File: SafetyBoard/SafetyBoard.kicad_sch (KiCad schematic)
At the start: 0 parts

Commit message: Changed a buncha stuff on other ppl's board. established new branch
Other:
- added sheet BSPD (../BSPD/BSPD/BSPD.kicad_sch)
- added sheet LATCH (../LATCH/LATCH/LATCH.kicad_sch)
- added sheet TSSI (../TSSI/TSSI/TSSI.kicad_sch)
- added sheet Untitled Sheet (../PDB/v2026.1/Kicad/PowerDistributionBoard.kicad_sch)

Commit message: day 2 grind
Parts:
- added F1, F2, F3, F4, F5, F6: ~, 0footprints:FUSE_3522-2, symbol Device:Fuse
- added J1: ESTOP/SDC switch, 0footprints:Molex_Mini-Fit_Jr_5566-02A_2x01_P4.20mm_Vertical, symbol Connector_Generic:Conn_02x01
- added J2, J3: SDC OUT, 0footprints:Molex_Mini-Fit_Jr_5566-02A_2x01_P4.20mm_Vertical, symbol Connector_Generic:Conn_02x01
- added J4, J7: ACCU, 0footprints:Molex_Mini-Fit_Jr_5566-04A_2x02_P4.20mm_Vertical, symbol Connector_Generic:Conn_02x02_Top_Bottom
- added J5: BSPD, 0footprints:Molex_Mini-Fit_Jr_5566-06A_2x03_P4.20mm_Vertical, symbol Connector_Generic:Conn_02x03_Top_Bottom
- added J6: LATCH, 0footprints:Molex_Mini-Fit_Jr_5566-08A_2x04_P4.20mm_Vertical, symbol Connector_Generic:Conn_02x04_Top_Bottom
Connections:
- net BSPD/12V: now also F1.1
- net LATCH/GVLM_OUTPUT: now also J1.1 (Pin_1)
- net TSSI/GLV: now also F5.1
- new net: F6.1, J4.1 (Pin_1)
- new net: J1.2 (Pin_2), J2.1 (Pin_1), J2.2 (Pin_2)
- new net 12V: F1.2, F2.2, F3.2, F5.2, F6.2
- new net 24V: F4.2, J3.1 (Pin_1)
- new net BMS FAULT: J4.4 (Pin_4)
- new net CCM Helper/12V: F3.1
- new net CCM Helper/24V: F4.1
- new net GND: J3.2 (Pin_2), J4.2 (Pin_2)
- new net IMD Fault: J4.3 (Pin_3)
- new net LATCH/12V: F2.1
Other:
- removed sheet Untitled Sheet
- added sheet CCM Helper (CCMIO.kicad_sch)
- added sheet DCDC CONVERTERS (./24V DC-DC Converter 2/24V DC-DC Converter.kicad_sch)
- sheet BSPD ports: added none; removed Current Sensor
- sheet LATCH ports: added 12V, IMD_FAULT; removed none
- sheet TSSI ports: added none; removed GREEN_LED, RED_LED

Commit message: hopefully this lets avadi pull
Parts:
- removed J5: BSPD, 0footprints:Molex_Mini-Fit_Jr_5566-06A_2x03_P4.20mm_Vertical, symbol Connector_Generic:Conn_02x03_Top_Bottom
- removed J6: LATCH, 0footprints:Molex_Mini-Fit_Jr_5566-08A_2x04_P4.20mm_Vertical, symbol Connector_Generic:Conn_02x04_Top_Bottom
- removed J7: ACCU, 0footprints:Molex_Mini-Fit_Jr_5566-04A_2x02_P4.20mm_Vertical, symbol Connector_Generic:Conn_02x02_Top_Bottom
- added F10, F7, F8, F9: ~, 0footprints:FUSE_3522-2, symbol Device:Fuse
- added J4, J7: 12v EXP, 0footprints:Molex_Mini-Fit_Jr_5566-02A_2x01_P4.20mm_Vertical, symbol Connector_Generic:Conn_02x01
- added J6: 24v EXP, 0footprints:Molex_Mini-Fit_Jr_5566-02A_2x01_P4.20mm_Vertical, symbol Connector_Generic:Conn_02x01
- J5: renamed from J3; value SDC OUT -> PWR IN
- renumbered J4 to J3
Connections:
- net 12V: now also F7.1
- net 24V: now also F8.1, F9.1; no longer J5.1 (Pin_1)
- net GND: now also J4.2 (Pin_2), J6.2 (Pin_2), J7.2 (Pin_2)
- new net: F7.2, J4.1 (Pin_1)
- new net: F9.2, J6.1 (Pin_1)
- new net: F8.2, J5.1 (Pin_1)
- new net: F10.2, J7.1 (Pin_1)
- new net 5V: F10.1
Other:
- sheet DCDC CONVERTERS ports: added 12V_OUT, 24V_IN, 5V; removed none
- moved on the sheet: J5

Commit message: rough layout done
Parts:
- J7: value 12v EXP -> 5v EXP
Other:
- sheet CCM Helper ports: added BPS1 OUT; removed BPS1_OUT
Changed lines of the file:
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@@
+	(wire
+		(pts
+			(xy 72.898 177.8) (xy 75.184 177.8)
+		)
+		(stroke
+			(width 0)
+			(type default)
+		)
+	)
 	(wire
 		(pts
@@
 		(pts
 			(xy 93.98 49.276) (xy 85.852 49.276)
-		)
-		(stroke
-			(width 0)
-			(type default)
-		)
-	)
-	(wire
-		(pts
-			(xy 74.93 177.8) (xy 72.898 177.8)
 		)
 		(stroke
@@
 	)
 	(label "24V"
+		(at 74.676 184.912 0)
+		(effects
+			(font
+				(size 1.27 1.27)
+			)
+			(justify left bottom)
+		)
+	)
+	(label "24V"
 		(at 228.854 33.02 180)
 		(effects
@@
 	)
 	(label "12V"
+		(at 75.184 177.8 0)
+		(effects
+			(font
+				(size 1.27 1.27)
+			)
+			(justify left bottom)
+		)
+	)
+	(label "12V"
 		(at 227.584 49.784 180)
 		(effects
@@
 		)
 	)
-	(label "24V"
-		(at 74.93 177.8 0)
-		(effects
-			(font
-				(size 1.27 1.27)
-			)
-			(justify left bottom)
-		)
-	)
 	(label "5V"
 		(at 72.898 180.848 0)
@@
 	)
 	(label "12V"
-		(at 74.676 184.912 0)
-		(effects
-			(font
-				(size 1.27 1.27)
-			)
-			(justify left bottom)
-		)
-	)
-	(label "12V"
 		(at 67.056 137.414 180)
 		(effects
@@
 			)
 		)
-		(property "Value" "12v EXP"
+		(property "Value" "5v EXP"
 			(at 243.078 59.182 0)
 			(effects
@@
 			)
 		)
-		(pin "BPS1_OUT" input
-			(at 93.98 49.276 180)
-			(effects
-				(font
-					(size 1.27 1.27)
-				)
-				(justify left)
-			)
-		)
 		(pin "CCM fdbk" input
 			(at 128.016 49.53 0)
@@
 			)
 		)
+		(pin "BPS1 OUT" input
+			(at 93.98 49.276 180)
+			(effects
+				(font
+					(size 1.27 1.27)
+				)
+				(justify left)
+			)
+		)

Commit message: silkscreen and some fuses or something
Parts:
- removed F1, F5: ~, 0footprints:FUSE_3522-2, symbol Device:Fuse
- added F1, F5: 2A, Fuse:Fuse_2920_7451Metric_Pad2.10x5.45mm_HandSolder, symbol Device:Polyfuse
- F3: value ~ -> 5A MAX
- F4, F8, F9: value ~ -> 10A MAX
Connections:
- net 12V: now also F1.1, F5.1
- net BSPD/12V: now also F1.2
- net TSSI/GLV: now also F5.2
- net at J1.2 (Pin_2), J2.2 (Pin_2): no longer J2.1 (Pin_1)
- no-connect marks 0 -> 1
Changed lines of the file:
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@@
 	(generator_version "9.0")
 	(paper "A4")
-	(junction
-		(at 152.908 140.208)
-		(diameter 0)
-		(color 0 0 0 0)
+	(no_connect
+		(at 154.432 140.208)
 	)
 	(wire
@@
 	(wire
 		(pts
-			(xy 154.432 140.208) (xy 152.908 140.208)
-		)
-		(stroke
-			(width 0)
-			(type default)
-		)
-	)
-	(wire
-		(pts
 			(xy 139.7 46.99) (xy 139.7 55.88)
 		)
@@
 		(pts
 			(xy 129.032 99.06) (xy 129.032 105.41)
+		)
+		(stroke
+			(width 0)
+			(type default)
+		)
+	)
+	(wire
+		(pts
+			(xy 46.99 71.374) (xy 47.244 71.374)
 		)
 		(stroke
@@
 	)
 	(label "12V"
-		(at 46.99 71.374 180)
+		(at 47.244 71.374 180)
 		(effects
 			(font
@@
 	(symbol
 		(lib_id "Device:Fuse")
-		(at 50.8 71.374 270)
-		(unit 1)
-		(exclude_from_sim no)
-		(in_bom yes)
-		(on_board yes)
-		(dnp no)
-		(property "Reference" "F1"
-			(at 50.8 73.66 90)
-			(effects
-				(font
-					(size 1.27 1.27)
-				)
-			)
-		)
-		(property "Value" "~"
-			(at 50.8 69.596 90)
-			(effects
-				(font
-					(size 1.27 1.27)
-				)
-			)
-		)
-		(property "Footprint" "0footprints:FUSE_3522-2"
-			(at 50.8 69.596 90)
-			(effects
-				(font
-					(size 1.27 1.27)
-				)
-				(hide yes)
-			)
-		)
-		(property "Datasheet" "https://www.keyelco.com/userAssets/file/M65p41.pdf"
-			(at 50.8 71.374 0)
-			(effects
-				(font
-					(size 1.27 1.27)
-				)
-				(hide yes)
-			)
-		)
-		(property "Description" "Fuse"
-			(at 50.8 71.374 0)
-			(effects
-				(font
-					(size 1.27 1.27)
-				)
-				(hide yes)
-			)
-		)
-		(pin "1"
-		)
-		(pin "2"
-		)
-		(instances
-			(project "SafetyBoard"
-				(path "/30d029c6-868b-41ac-953d-167a7d76c1a3"
-					(reference "F1")
-					(unit 1)
-				)
-			)
-		)
-	)
-	(symbol
-		(lib_id "Device:Fuse")
 		(at 210.566 125.73 270)
 		(unit 1)
@@
 			)
 		)
-		(property "Value" "~"
+		(property "Value" "10A MAX"
 			(at 131.826 37.846 90)
 			(effects
@@
 	)
 	(symbol
+		(lib_id "Device:Polyfuse")
+		(at 180.086 67.056 270)
+		(unit 1)
+		(exclude_from_sim no)
+		(in_bom yes)
+		(on_board yes)
+		(dnp no)
+		(fields_autoplaced yes)
+		(property "Reference" "F5"
+			(at 180.086 61.214 90)
+			(effects
+				(font
+					(size 1.27 1.27)
+				)
+			)
+		)
+		(property "Value" "2A"
+			(at 180.086 63.754 90)
+			(effects
+				(font
+					(size 1.27 1.27)
+				)
+			)
+		)
+		(property "Footprint" "Fuse:Fuse_2920_7451Metric_Pad2.10x5.45mm_HandSolder"
+			(at 175.006 68.326 0)
+			(effects
+				(font
+					(size 1.27 1.27)
+				)
+				(justify left)
+				(hide yes)
+			)
+		)
+		(property "Datasheet" "~"
+			(at 180.086 67.056 0)
+			(effects
+				(font
+					(size 1.27 1.27)
+				)
+				(hide yes)
+			)
+		)
+		(property "Description" "Resettable fuse, polymeric positive temperature coefficient"
+			(at 180.086 67.056 0)
+			(effects
+				(font
+					(size 1.27 1.27)
+				)
+				(hide yes)
+			)
+		)
+		(property "MPN" "SMD2920B200TF/24 "
+			(at 180.086 67.056 0)
+			(effects
+				(font
+					(size 1.27 1.27)
+				)
+				(hide yes)
+			)
+		)
+		(property "MFG" "YAGEO"
+			(at 180.086 67.056 0)
+			(effects
+				(font
+					(size 1.27 1.27)
+				)
+				(hide yes)
+			)
+		)
+		(pin "2"
+		)
+		(pin "1"
+		)
+		(instances
+			(project "SafetyBoard"
+				(path "/30d029c6-868b-41ac-953d-167a7d76c1a3"
+					(reference "F5")
+					(unit 1)
+				)
+			)
+		)
+	)
+	(symbol
 		(lib_id "power:GND")
 		(at 248.412 17.272 0)
@@
 			)
 		)
-		(property "Value" "~"
+		(property "Value" "5A MAX"
 			(at 131.826 33.274 90)
 			(effects
@@
 			)
 		)
-		(property "Value" "~"
+		(property "Value" "10A MAX"
 			(at 231.902 19.05 90)
 			(effects
@@
 	)
 	(symbol
-		(lib_id "Device:Fuse")
-		(at 180.086 67.056 90)
-		(unit 1)
-		(exclude_from_sim no)
-		(in_bom yes)
-		(on_board yes)
-		(dnp no)
-		(property "Reference" "F5"
-			(at 180.086 64.77 90)
-			(effects
-				(font
-					(size 1.27 1.27)
-				)
-			)
-		)
-		(property "Value" "~"
-			(at 180.086 68.834 90)
-			(effects
-				(font
-					(size 1.27 1.27)
-				)
-			)
-		)
-		(property "Footprint" "0footprints:FUSE_3522-2"
-			(at 180.086 68.834 90)
-			(effects
-				(font
-					(size 1.27 1.27)
-				)
-				(hide yes)
-			)
-		)
-		(property "Datasheet" "https://www.keyelco.com/userAssets/file/M65p41.pdf"
-			(at 180.086 67.056 0)
-			(effects
-				(font
-					(size 1.27 1.27)
-				)
-				(hide yes)
-			)
-		)
-		(property "Description" "Fuse"
-			(at 180.086 67.056 0)
-			(effects
-				(font
-					(size 1.27 1.27)
-				)
-				(hide yes)
-			)
-		)
-		(pin "1"
-		)
-		(pin "2"
-		)
-		(instances
-			(project "SafetyBoard"
-				(path "/30d029c6-868b-41ac-953d-167a7d76c1a3"
-					(reference "F5")
-					(unit 1)
-				)
-			)
-		)
-	)
-	(symbol
 		(lib_id "Connector_Generic:Conn_02x01")
 		(at 240.792 17.272 0)
@@
 			)
 		)
-		(property "Value" "~"
+		(property "Value" "10A MAX"
 			(at 232.664 34.798 90)
 			(effects
@@
 					(unit 1)
 				)
+			)
+		)
+	)
+	(symbol
+		(lib_id "Device:Polyfuse")
+		(at 50.8 71.374 90)
+		(unit 1)
+		(exclude_from_sim no)
+		(in_bom yes)
+		(on_board yes)
+		(dnp no)
+		(fields_autoplaced yes)
+		(property "Reference" "F1"
+			(at 50.8 64.77 90)
+			(effects
+				(font
+					(size 1.27 1.27)
+				)
+			)
+		)
+		(property "Value" "2A"
+			(at 50.8 67.31 90)
+			(effects
+				(font
+					(size 1.27 1.27)
+				)
+			)
+		)
+		(property "Footprint" "Fuse:Fuse_2920_7451Metric_Pad2.10x5.45mm_HandSolder"
+			(at 55.88 70.104 0)
+			(effects
+				(font
+					(size 1.27 1.27)
+				)
+				(justify left)
+				(hide yes)
+			)
+		)
+		(property "Datasheet" "~"
+			(at 50.8 71.374 0)
+			(effects
+				(font
+					(size 1.27 1.27)
+				)
+				(hide yes)
+			)
+		)
+		(property "Description" "Resettable fuse, polymeric positive temperature coefficient"
+			(at 50.8 71.374 0)
+			(effects
+				(font
+					(size 1.27 1.27)
+				)
+				(hide yes)
+			)
+		)
+		(property "MPN" "SMD2920B200TF/24 "
+			(at 50.8 71.374 0)
+			(effects
+				(font
+					(size 1.27 1.27)
+				)
+				(hide yes)
+			)
+		)
+		(property "MFG" "YAGEO"
+			(at 50.8 71.374 0)
+			(effects
+				(font
+					(size 1.27 1.27)
+				)
+				(hide yes)
+			)
+		)
+		(pin "2"
+		)
+		(pin "1"
+		)
+		(instances
+			(project "SafetyBoard"
+				(path "/30d029c6-868b-41ac-953d-167a7d76c1a3"
+					(reference "F1")
+					(unit 1)
+				)

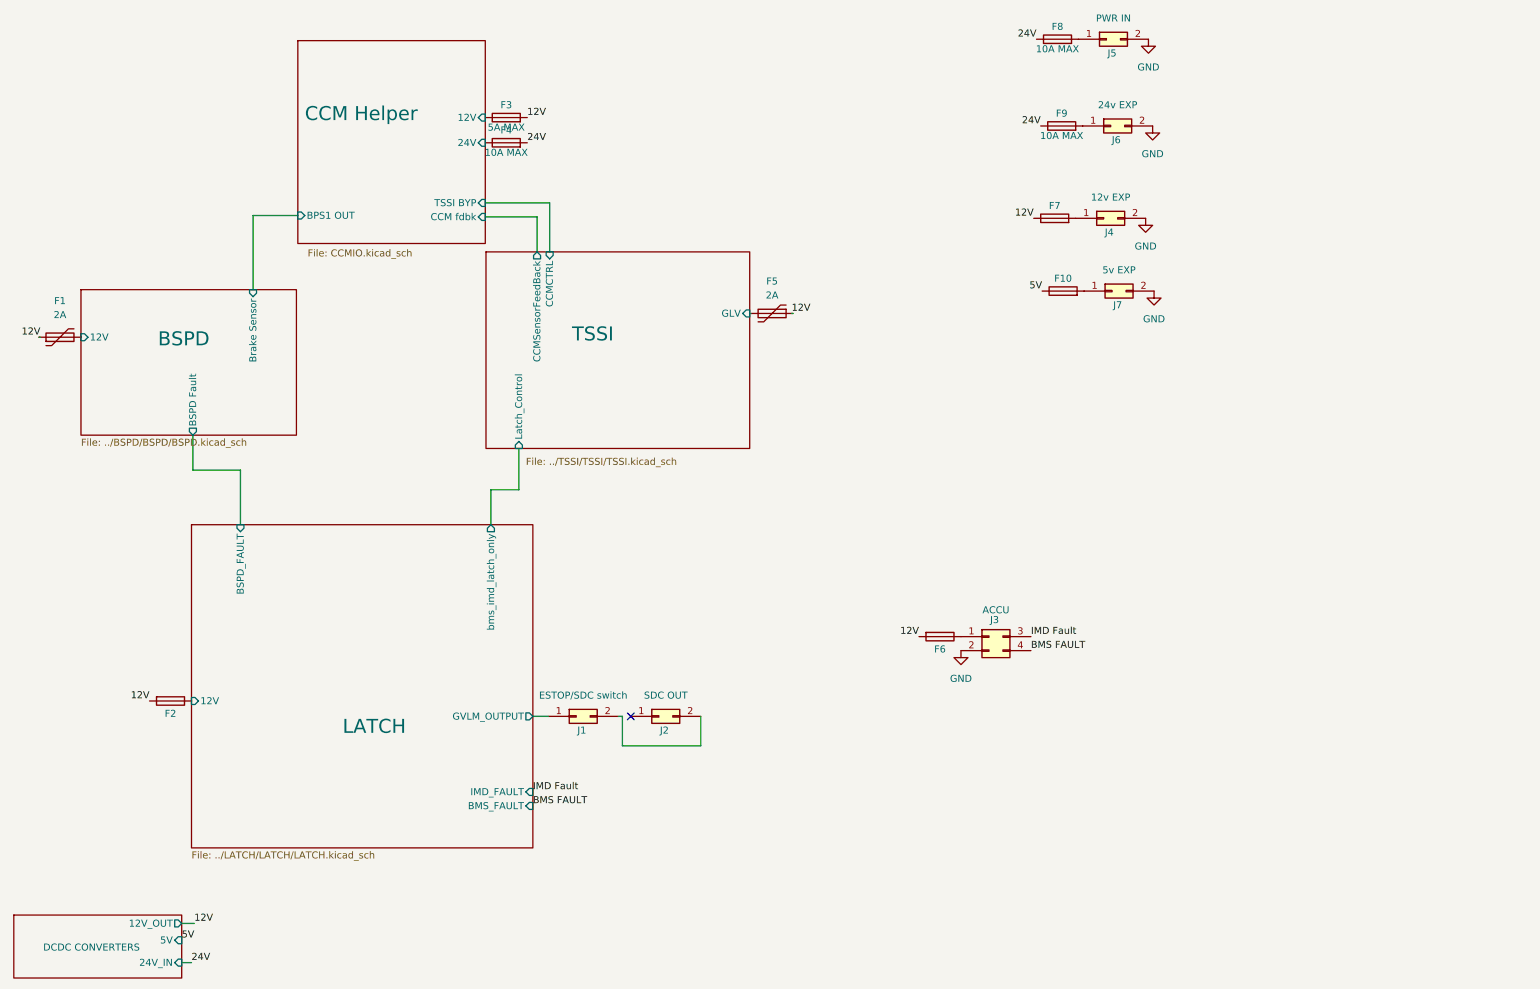
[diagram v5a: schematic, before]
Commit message: I think think this is final but need to defuck the BOM
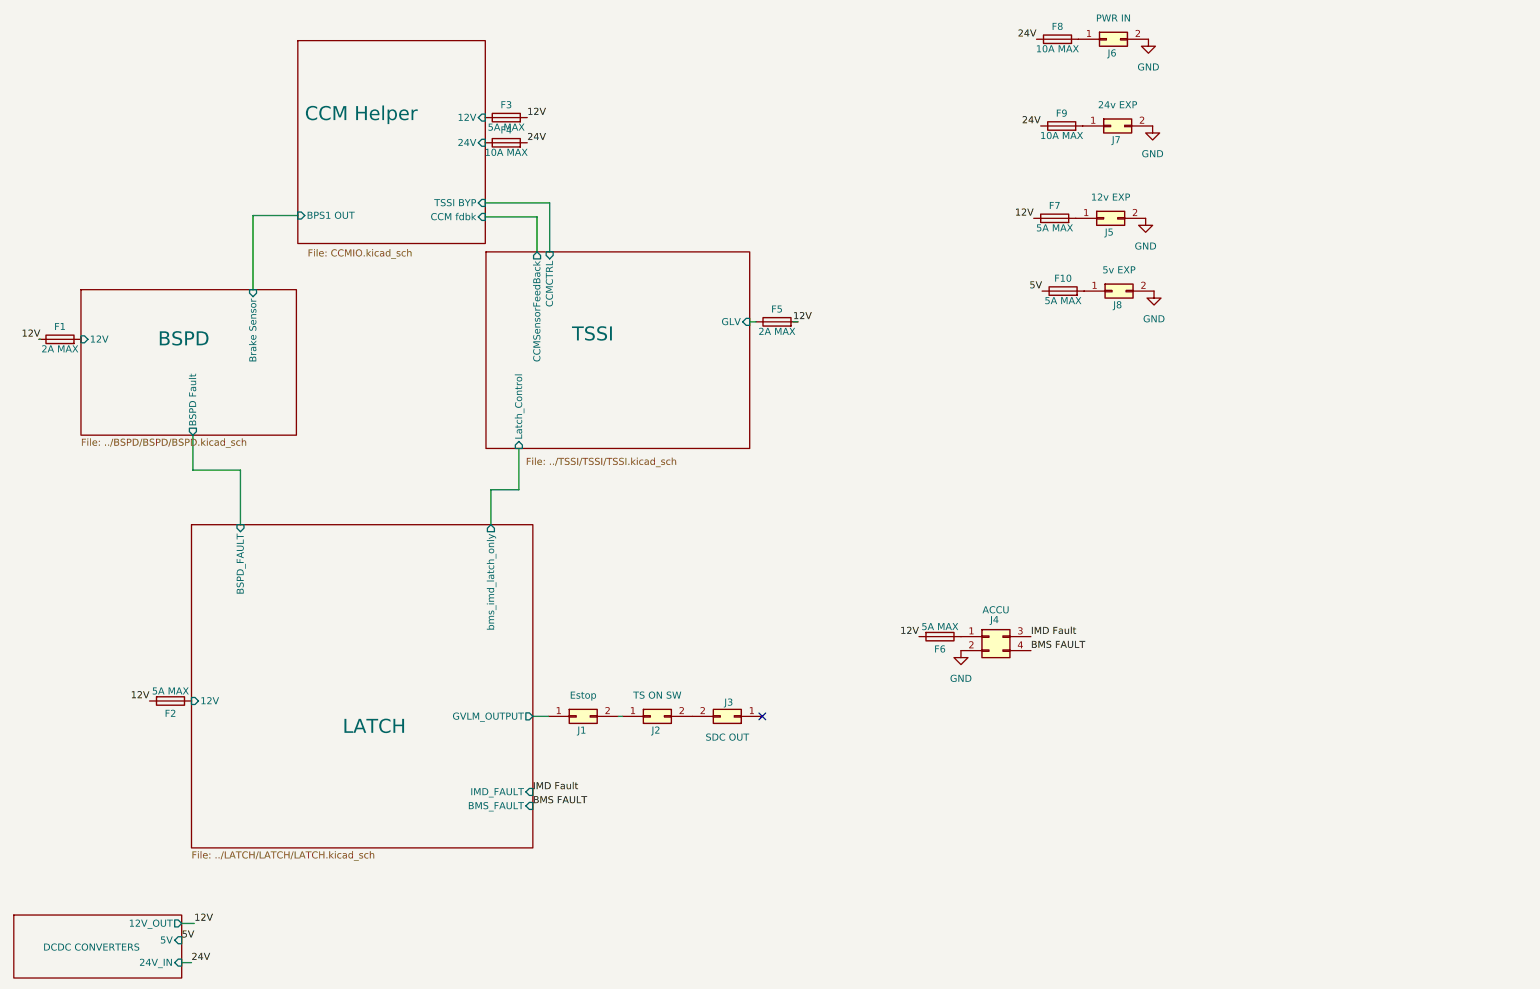
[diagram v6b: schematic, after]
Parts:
- removed F1, F5: 2A, Fuse:Fuse_2920_7451Metric_Pad2.10x5.45mm_HandSolder, symbol Device:Polyfuse
- added F1, F5: 2A MAX, 0footprints:FUSE_3522-2, symbol Device:Fuse
- added J2: TS ON SW, 0footprints:Molex_Mini-Fit_Jr_5566-02A_2x01_P4.20mm_Vertical, symbol Connector_Generic:Conn_02x01
- F10, F2, F6, F7: value ~ -> 5A MAX
- J1: value ESTOP/SDC switch -> Estop
- renumbered J2 to J3, J3 to J4, J4 to J5, J5 to J6, J6 to J7, J7 to J8
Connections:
- net 12V: now also F1.1, F5.2
- net BSPD/12V: now also F1.2
- net TSSI/GLV: now also F5.1
- net at J1.2 (Pin_2): now also J2.1 (Pin_1); no longer J3.2 (Pin_2)
- new net: J2.2 (Pin_2), J3.2 (Pin_2)
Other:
- moved on the sheet: J3

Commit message: Safety Board: added BOM and updated schematics
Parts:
- F1, F10, F2, F3, F4, F5, F6, F7, F8, F9: MFG (none) -> Littelfuse; MPN (none) -> 01530007Z
- J1, J2, J3, J5, J6, J7, J8: MFG (none) -> Molex; MPN (none) -> 0039310028
- J4: MFG (none) -> Molex; MPN (none) -> 0039288040

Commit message: updates I think
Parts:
- F1, F10, F2, F5, F6, F7, F8, F9: MFG Littelfuse -> Keystone Electronics; MPN 01530007Z -> 3522-2
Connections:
- net 12V: now also F2.1, F6.1; no longer F2.2, F6.2
- net LATCH/12V: now also F2.2; no longer F2.1
- net at J4.1 (Pin_1): now also F6.2; no longer F6.1
